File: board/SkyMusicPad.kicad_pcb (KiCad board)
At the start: 4 copper layers, 130 x 62.5 mm, 52 parts, among them SW1 Cherry, SW10 Cherry, SW11 Cherry, SW12 Cherry, SW13 Cherry, SW14 Cherry, SW15 Cherry, SW16 RotaryEncoder_Switch, SW2 Cherry, SW3 Cherry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

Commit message: Fix minor issues, adjust diode silkscreen
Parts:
- D1, D10, D11, D12, D13, D14, D15, D2, D3, D4, D5, D6, D7, D8, D9: footprint Diode_SMD:D_MiniMELF -> SkyMusic:D_MiniMELF_silkMoved

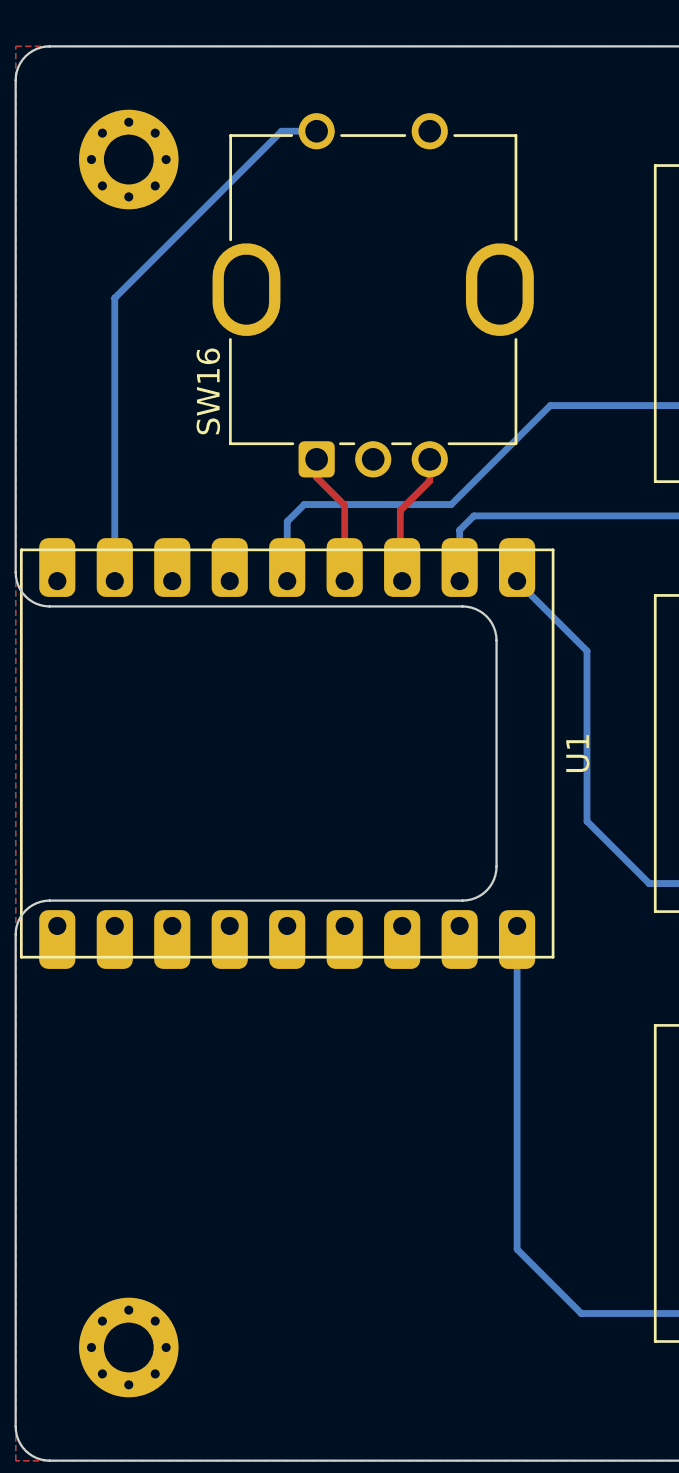
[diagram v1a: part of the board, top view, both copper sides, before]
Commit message: Adjusted LED silk, need to fix encoder
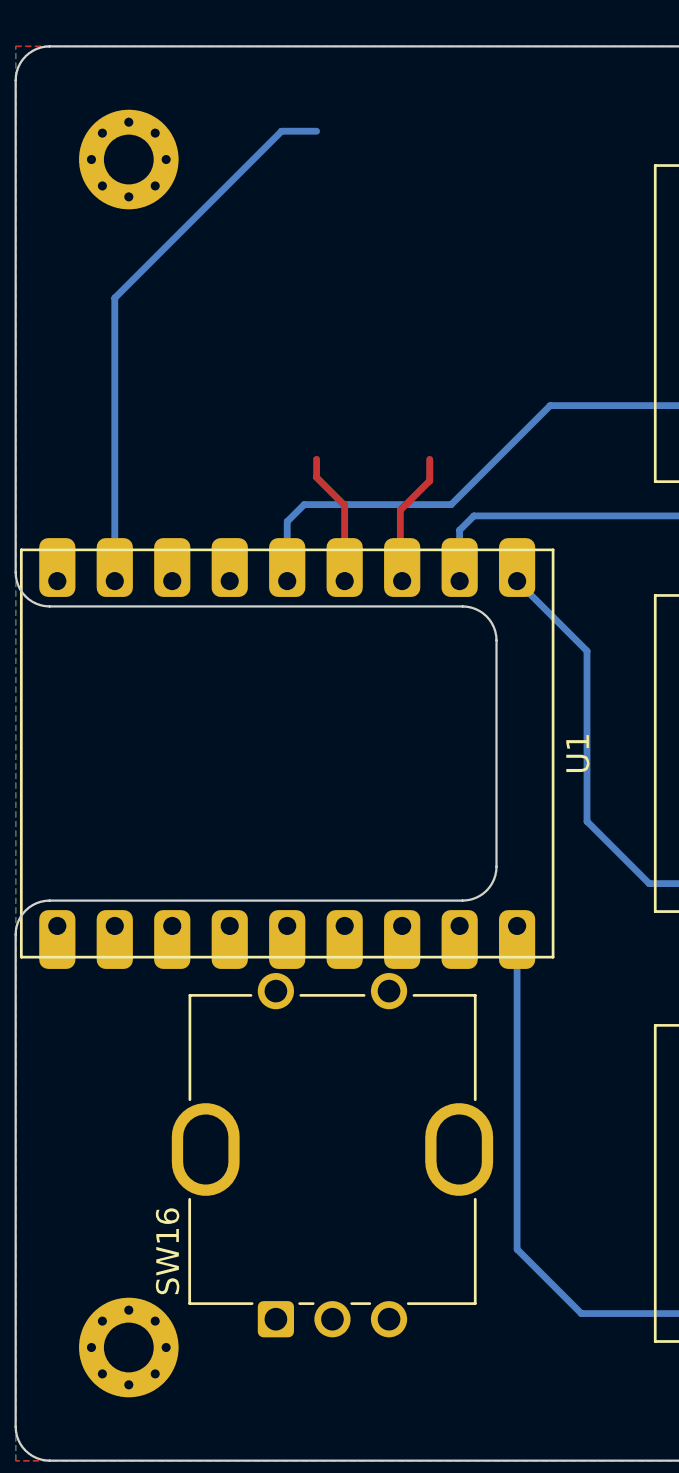
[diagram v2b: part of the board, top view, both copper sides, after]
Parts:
- moved SW16 38.0 mm to (51.2, 80.0)
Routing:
- net Col4: track 177.3 -> 151.8 mm
- net Col3: track 153.4 -> 129.0 mm
- net Col2: track 131.2 -> 107.8 mm
- net Col1: track 109.0 -> 86.8 mm
- net Col0: track 86.2 -> 64.6 mm

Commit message: misc updates
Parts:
- SW16: footprint Rotary_Encoder:RotaryEncoder_Bourns_Vertical_PEC12R-3x17F-Sxxxx -> SkyMusic:RotaryEncoder_Bourns_Vertical_PEC12R-3x17F-Sxxxx
- moved SW16 6.96 mm to (53.8, 73.5), turned to 180 degrees
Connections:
- SW16 pad A: Rot_A -> Rot_B
- SW16 pad B: Rot_B -> Rot_A
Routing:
- net Rot_A: track 5.89 -> 48.4 mm
- net Rot_SW: track 24.5 -> 63.9 mm
- net Rot_B: track 5.95 -> 36.8 mm
- net Col4: track 151.8 -> 178.6 mm
- net Col3: track 129.0 -> 153.4 mm
- net Col2: track 107.8 -> 131.9 mm
- net Col1: track 86.8 -> 108.9 mm
- net Col0: track 64.6 -> 60.8 mm

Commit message: Components placed
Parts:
- removed H4: GND, MountingHole:MountingHole_2.2mm_M2_Pad_Via
- removed REF**: OSHW-Logo2_7.3x6mm_Copper, Symbol:OSHW-Logo2_7.3x6mm_Copper
- added J1: Conn_01x04, SkyMusic:OLED_DFR0648, F.Cu at (83.0, 59.0)
- moved H3 153.5 mm to (195.0, 50.0)
- moved H2 86.7 mm to (195.0, 110.0)
- moved H1 85.1 mm to (70.0, 110.0)
- moved SW15 43.2 mm to (186.2, 99.0)
- moved SW14 43.2 mm to (186.2, 80.0)
- moved SW12 43.2 mm to (167.2, 99.0)
- moved SW13 43.1 mm to (186.2, 61.0)
- moved SW11 43.1 mm to (167.2, 80.0)
- moved SW9 43.1 mm to (148.1, 99.0)
- moved SW10 43.1 mm to (167.2, 61.0)
- moved SW8 43.1 mm to (148.1, 80.0)
- moved SW6 43.1 mm to (129.1, 99.0)
- moved SW7 43.1 mm to (148.1, 61.0)
- moved D30 43.1 mm to (186.2, 103.3)
- moved SW5 43.1 mm to (129.1, 80.0)
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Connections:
- U1 pad 1: unconnected-(U1-TX-Pad1) -> +5V
- U1 pad 10: Row2 -> unconnected-(U1-GP7-Pad10)
- U1 pad 11: Col0 -> Neopixel
- U1 pad 12: Col1 -> Row2
- U1 pad 13: Col2 -> Row1
- U1 pad 14: Col3 -> Row0
- U1 pad 15: Col4 -> SDA
- U1 pad 16: +3.3V -> SCL
- U1 pad 17: GND -> unconnected-(U1-RX-Pad17)
- U1 pad 18: +5V -> unconnected-(U1-TX-Pad18)
- U1 pad 2: Rot_SW -> GND
- U1 pad 3: SDA -> +3.3V
- U1 pad 4: SCL -> Col4
- U1 pad 5: Neopixel -> Col3
- U1 pad 6: Rot_A -> Col2
- U1 pad 7: Rot_B -> Col1
- U1 pad 8: Row0 -> Col0
- U1 pad 9: Row1 -> unconnected-(U1-GP6-Pad9)
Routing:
- net Col4: track 178.6 -> 0.00 mm
- net Col3: track 153.4 -> 0.00 mm
- net Col2: track 131.9 -> 0.00 mm
- net Row2: track 110.9 -> 0.00 mm, vias 5 -> 0
- net Col1: track 108.9 -> 0.00 mm
- net Row1: track 105.3 -> 0.00 mm, vias 5 -> 0
- net Row0: track 100.6 -> 0.00 mm, vias 5 -> 0
- net Row0_out: track 92.2 -> 0.00 mm, vias 2 -> 0
- net Row1_out: track 91.2 -> 0.00 mm, vias 2 -> 0
- net Rot_SW: track 63.9 -> 0.00 mm
- net Col0: track 60.8 -> 0.00 mm
- net Rot_A: track 48.4 -> 0.00 mm
- net Rot_B: track 36.8 -> 0.00 mm
- net Neopixel: track 25.8 -> 0.00 mm
- net Net-(D29-DOUT): track 15.2 -> 0.00 mm
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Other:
- board size 130 x 62.5 mm -> 135 x 70 mm
- board text removed: "Designed by @voxeltek and @citacritta Assembled by hand in Australia This is an unnofficial community project"

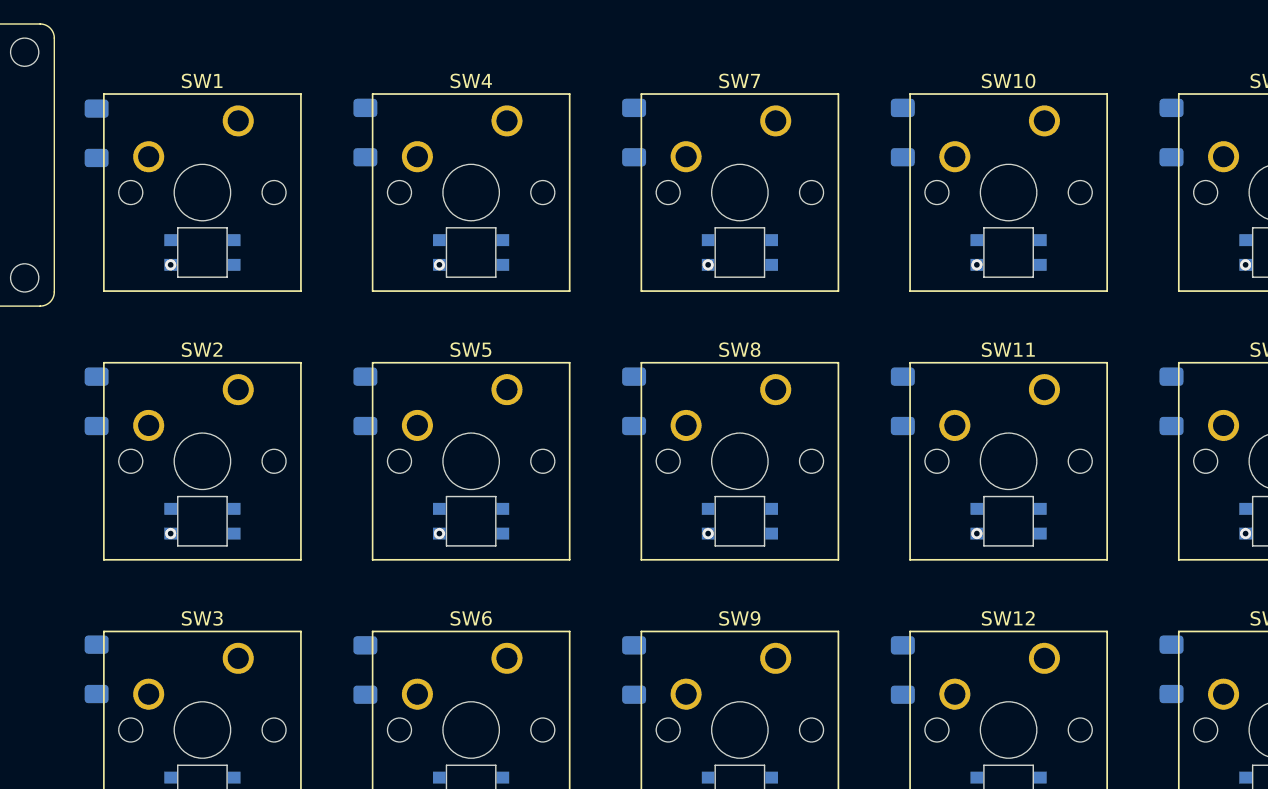
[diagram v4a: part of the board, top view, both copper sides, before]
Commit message: Slight placement adjustments
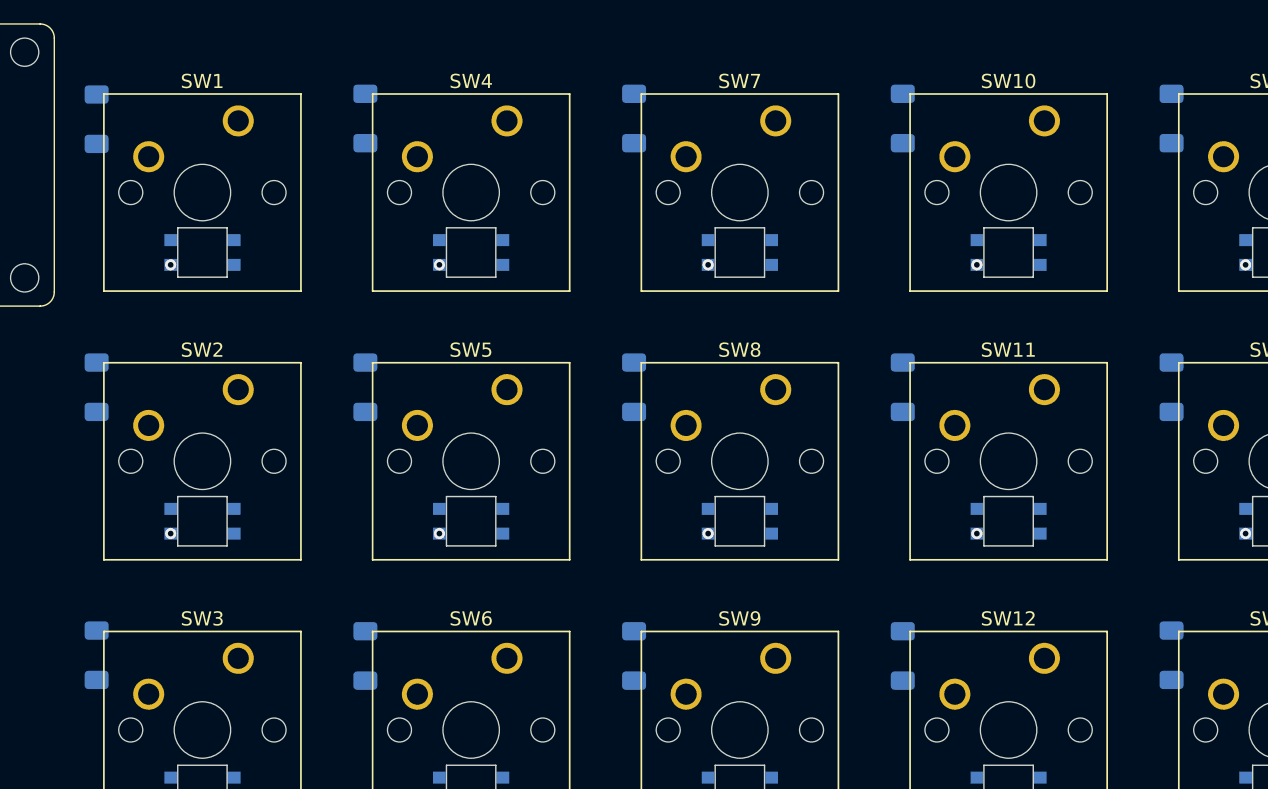
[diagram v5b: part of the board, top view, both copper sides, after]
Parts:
- moved D1 1.00 mm to (102.5, 55.8)
- moved D10 1.00 mm to (159.7, 55.7)
- moved D11 1.00 mm to (159.7, 74.8)
- moved D12 1.00 mm to (159.7, 93.8)
- moved D13 1.00 mm to (178.7, 55.7)
- moved D14 1.00 mm to (178.7, 74.8)
- moved D15 1.00 mm to (178.7, 93.8)
- moved D2 1.00 mm to (102.5, 74.8)
- moved D3 1.00 mm to (102.5, 93.8)
- moved D4 1.00 mm to (121.5, 55.7)
- moved D5 1.00 mm to (121.5, 74.8)
- moved D6 1.00 mm to (121.5, 93.8)
- moved D7 1.00 mm to (140.6, 55.7)
- moved D8 1.00 mm to (140.6, 74.8)
- moved D9 1.00 mm to (140.6, 93.8)
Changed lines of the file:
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@@
 	(footprint "SkyMusic:D_MiniMELF_silkMoved"
 		(layer "B.Cu")
-		(at 140.6 56.7 -90)
+		(at 140.6 55.7 -90)
 		(descr "Diode Mini-MELF (SOD-80)")
 		(tags "Diode Mini-MELF (SOD-80)")
@@
 	(footprint "SkyMusic:D_MiniMELF_silkMoved"
 		(layer "B.Cu")
-		(at 102.5 94.75 -90)
+		(at 102.5 93.75 -90)
 		(descr "Diode Mini-MELF (SOD-80)")
 		(tags "Diode Mini-MELF (SOD-80)")
@@
 	(footprint "SkyMusic:D_MiniMELF_silkMoved"
 		(layer "B.Cu")
-		(at 121.55 75.75 -90)
+		(at 121.55 74.75 -90)
 		(descr "Diode Mini-MELF (SOD-80)")
 		(tags "Diode Mini-MELF (SOD-80)")
@@
 	(footprint "SkyMusic:D_MiniMELF_silkMoved"
 		(layer "B.Cu")
-		(at 178.7 75.75 -90)
+		(at 178.7 74.75 -90)
 		(descr "Diode Mini-MELF (SOD-80)")
 		(tags "Diode Mini-MELF (SOD-80)")
@@
 	(footprint "SkyMusic:D_MiniMELF_silkMoved"
 		(layer "B.Cu")
-		(at 178.7 94.75 -90)
+		(at 178.7 93.75 -90)
 		(descr "Diode Mini-MELF (SOD-80)")
 		(tags "Diode Mini-MELF (SOD-80)")
@@
 	(footprint "SkyMusic:D_MiniMELF_silkMoved"
 		(layer "B.Cu")
-		(at 121.55 56.7 -90)
+		(at 121.55 55.7 -90)
 		(descr "Diode Mini-MELF (SOD-80)")
 		(tags "Diode Mini-MELF (SOD-80)")
@@
 	(footprint "SkyMusic:D_MiniMELF_silkMoved"
 		(layer "B.Cu")
-		(at 159.65 56.7 -90)
+		(at 159.65 55.7 -90)
 		(descr "Diode Mini-MELF (SOD-80)")
 		(tags "Diode Mini-MELF (SOD-80)")
@@
 	(footprint "SkyMusic:D_MiniMELF_silkMoved"
 		(layer "B.Cu")
-		(at 178.7 56.7 -90)
+		(at 178.7 55.7 -90)
 		(descr "Diode Mini-MELF (SOD-80)")
 		(tags "Diode Mini-MELF (SOD-80)")
@@
 	(footprint "SkyMusic:D_MiniMELF_silkMoved"
 		(layer "B.Cu")
-		(at 102.5 75.75 -90)
+		(at 102.5 74.75 -90)
 		(descr "Diode Mini-MELF (SOD-80)")
 		(tags "Diode Mini-MELF (SOD-80)")
@@
 	(footprint "SkyMusic:D_MiniMELF_silkMoved"
 		(layer "B.Cu")
-		(at 140.6 75.75 -90)
+		(at 140.6 74.75 -90)
 		(descr "Diode Mini-MELF (SOD-80)")
 		(tags "Diode Mini-MELF (SOD-80)")
@@
 	(footprint "SkyMusic:D_MiniMELF_silkMoved"
 		(layer "B.Cu")
-		(at 159.65 75.75 -90)
+		(at 159.65 74.75 -90)
 		(descr "Diode Mini-MELF (SOD-80)")
 		(tags "Diode Mini-MELF (SOD-80)")
@@
 	(footprint "SkyMusic:D_MiniMELF_silkMoved"
 		(layer "B.Cu")
-		(at 102.5 56.75 -90)
+		(at 102.5 55.75 -90)
 		(descr "Diode Mini-MELF (SOD-80)")
 		(tags "Diode Mini-MELF (SOD-80)")
@@
 	(footprint "SkyMusic:D_MiniMELF_silkMoved"
 		(layer "B.Cu")
-		(at 140.6 94.8 -90)
+		(at 140.6 93.8 -90)
 		(descr "Diode Mini-MELF (SOD-80)")
 		(tags "Diode Mini-MELF (SOD-80)")
@@
 	(footprint "SkyMusic:D_MiniMELF_silkMoved"
 		(layer "B.Cu")
-		(at 159.65 94.8 -90)
+		(at 159.65 93.8 -90)
 		(descr "Diode Mini-MELF (SOD-80)")
 		(tags "Diode Mini-MELF (SOD-80)")
@@
 	(footprint "SkyMusic:D_MiniMELF_silkMoved"
 		(layer "B.Cu")
-		(at 121.55 94.8 -90)
+		(at 121.55 93.8 -90)
 		(descr "Diode Mini-MELF (SOD-80)")
 		(tags "Diode Mini-MELF (SOD-80)")
@@
 	)
 	(group ""
-		(members "16b4b028-9e51-4dd1-b3e1-b1dd38e565ca" "1978eea1-720a-494c-8d3c-70cddbe3d729"
-			"20054213-4c01-4d4e-8036-8e927ef5249a" "2592fc73-b78c-4348-905e-e52a71ae1b10"
-			"2a480e56-2350-4230-ba34-c0e7b8f6ed58" "536344b1-27b4-4450-82d1-7444ec4bedf6"
-			"53dbeaea-8919-4fea-8a0e-659b4755f966" "66ca874e-4dbd-4534-981c-61c31156ed87"
-			"7c398c85-7832-49d4-a7a7-828dd2988209" "8475f61f-2982-44b0-8377-02f896c06f99"
-			"c36fa7df-0446-43c7-94f2-1ccabdd618df" "c849bea5-11d2-4a9f-9f4d-b40a77c52475"
-			"cb1bfb6f-5c73-4d01-9a59-8bcb1b450801" "dee088e9-0133-413b-abb7-5496bd2b6e24"
-			"e5c75143-e57d-415d-a088-22c8b2cdfbc8" "fd73b79e-89a6-45a1-98ca-10d401f35e1f"
-		)
-	)
-	(group ""
 		(members "1b88897b-b963-4d54-8fef-2f648ed67648" "21df162e-8fbe-4495-990d-cacf4fb4ac4a"
 			"2786c1b2-7b63-4df9-9fb0-831e5beb0036" "475dc76f-1c4f-4120-80df-8099f5c70716"
@@
 		)
 	)
+	(group ""
+		(members "16b4b028-9e51-4dd1-b3e1-b1dd38e565ca" "1978eea1-720a-494c-8d3c-70cddbe3d729"
+			"20054213-4c01-4d4e-8036-8e927ef5249a" "2592fc73-b78c-4348-905e-e52a71ae1b10"
+			"2a480e56-2350-4230-ba34-c0e7b8f6ed58" "536344b1-27b4-4450-82d1-7444ec4bedf6"
+			"53dbeaea-8919-4fea-8a0e-659b4755f966" "7c398c85-7832-49d4-a7a7-828dd2988209"
+			"8475f61f-2982-44b0-8377-02f896c06f99" "c36fa7df-0446-43c7-94f2-1ccabdd618df"
+			"c849bea5-11d2-4a9f-9f4d-b40a77c52475" "cb1bfb6f-5c73-4d01-9a59-8bcb1b450801"
+			"dee088e9-0133-413b-abb7-5496bd2b6e24" "e5c75143-e57d-415d-a088-22c8b2cdfbc8"
+			"fd73b79e-89a6-45a1-98ca-10d401f35e1f"
+		)
+	)
